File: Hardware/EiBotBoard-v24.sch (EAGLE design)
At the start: 99 parts, among them IC1 A4988ALT1, IC2 A4988ALT1, IC3 PIC18F46J50-I/PT, IC4 V_REG_317DPACK, IC5 V_REG_317DPACK

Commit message: Updated board and schematic as per Peter Lewis' design review nodes (issue #1 in GitHub)
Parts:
- renumbered IC1 to U1, IC2 to U2, IC3 to U3, IC4 to U4, IC5 to U5
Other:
- note added: "Updated as per SparkFun design review #1 (issue 1)"
- note added: "copyright 2011-2015"
- note added: "of Schmalz Haus LLC"
- note added: "v2.4 04/29/2015 - Revision by BPS"
- note removed: "copyright 2011-2013"
- note removed: "of Schmalz Haus"

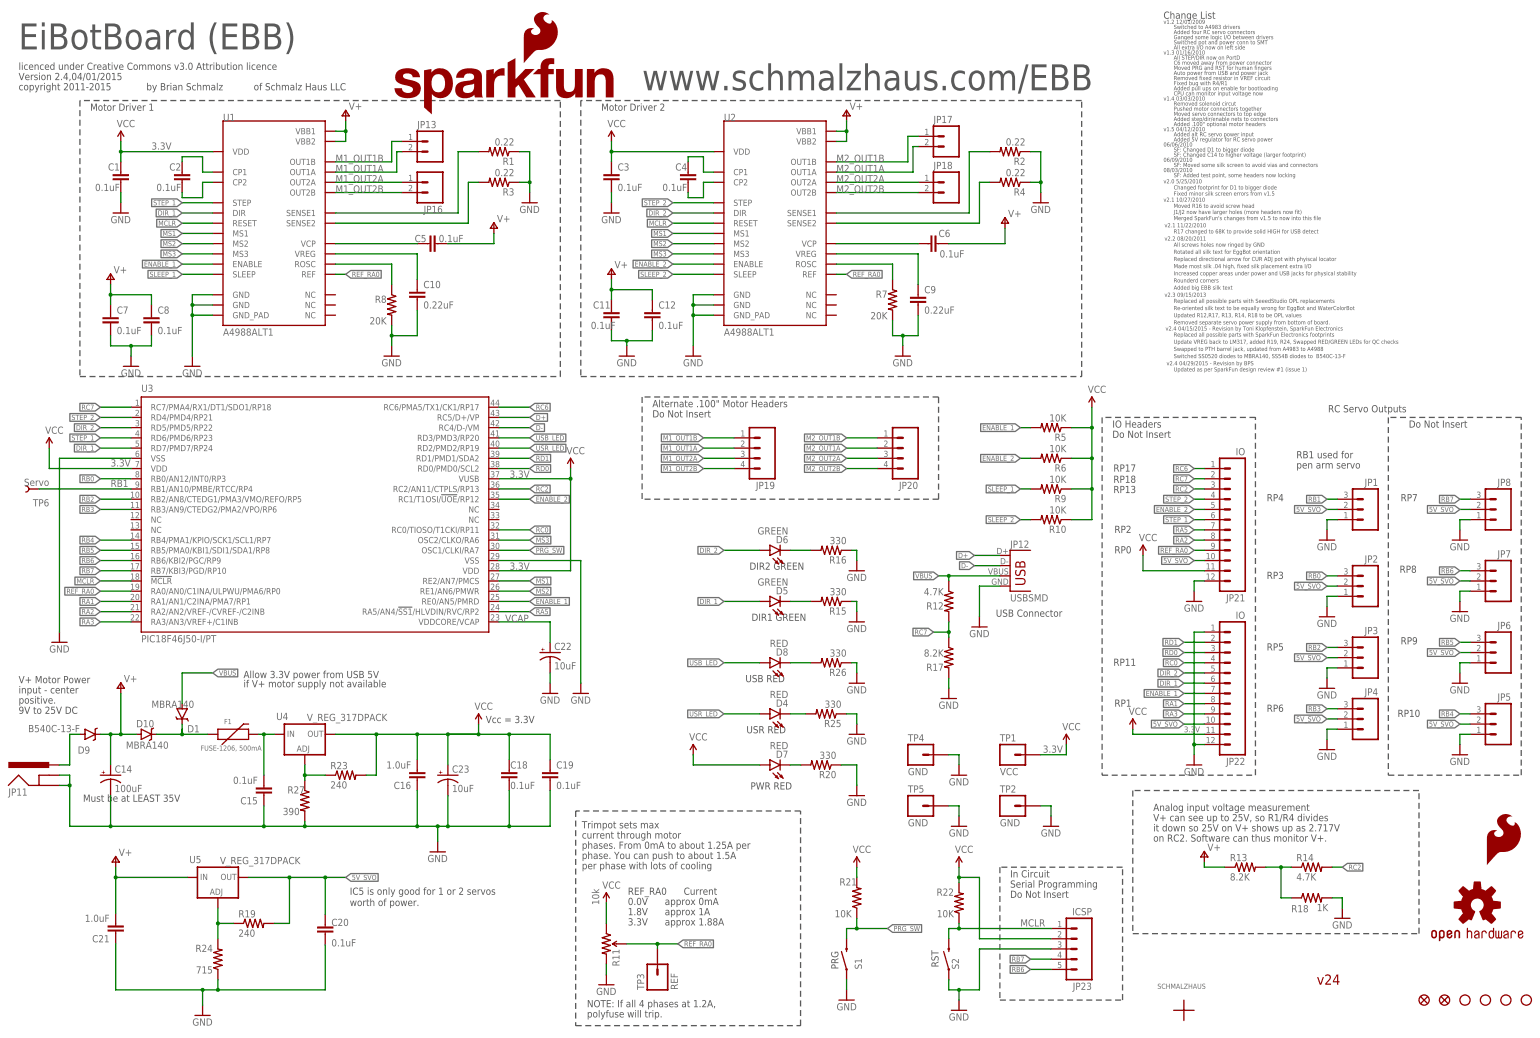
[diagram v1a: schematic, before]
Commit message: Reverted LEDs back to their original colors, removed outline line on tPlace, made outline on dimension layer 0.008" wide, switched driver chip footprints to A4988ALT1_REDUCED_PASTE.
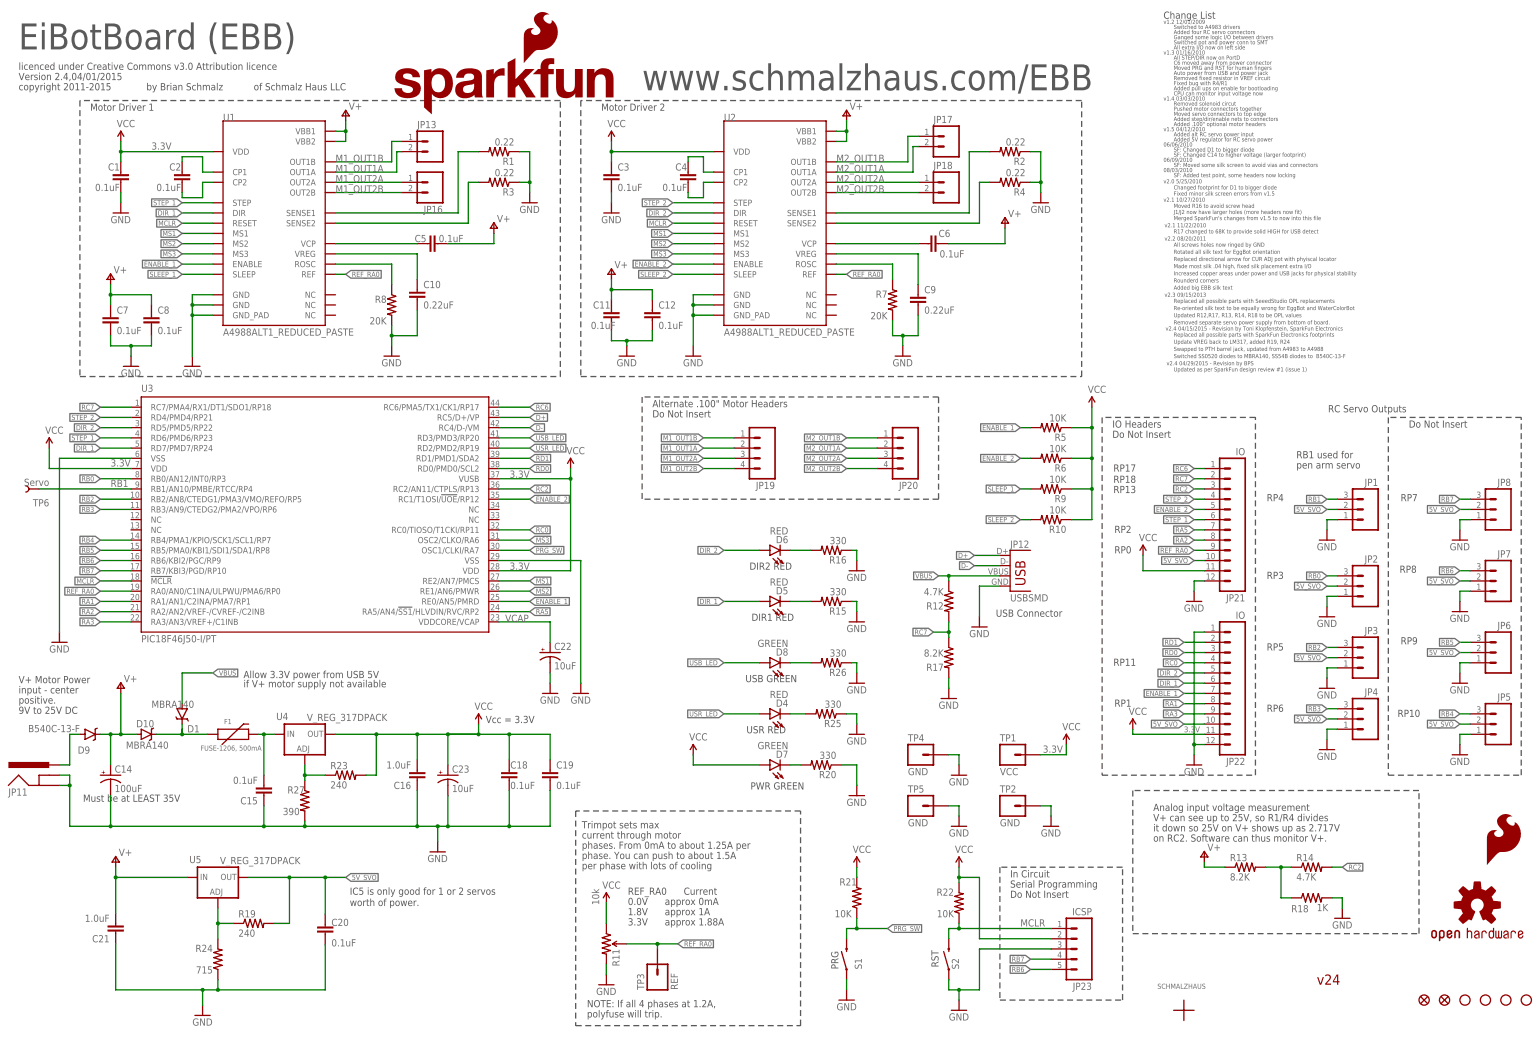
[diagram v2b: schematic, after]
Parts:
- D5, D6: value GREEN -> RED; device SparkFun-LED:LED-GREEN0603 -> SparkFun-LED:LED-RED0603
- D7, D8: value RED -> GREEN; device SparkFun-LED:LED-RED0603 -> SparkFun-LED:LED-GREEN0603
- U1, U2: value A4988ALT1 -> A4988ALT1_REDUCED_PASTE; device SparkFun-PowerIC:A4988ALT1 -> SparkFun-PowerIC:A4988ALT1_REDUCED_PASTE
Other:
- note added: "DIR1 RED"
- note added: "DIR2 RED"
- note added: "PWR GREEN"
- note added: "USB GREEN"
- note added: "Update VREG back to LM317, added R19, R24"
- note removed: "DIR1 GREEN"
- note removed: "DIR2 GREEN"
- note removed: "PWR RED"
- note removed: "USB RED"
- note removed: "Update VREG back to LM317, added R19, R24, Swapped RED/GREEN LEDs for QC checks"

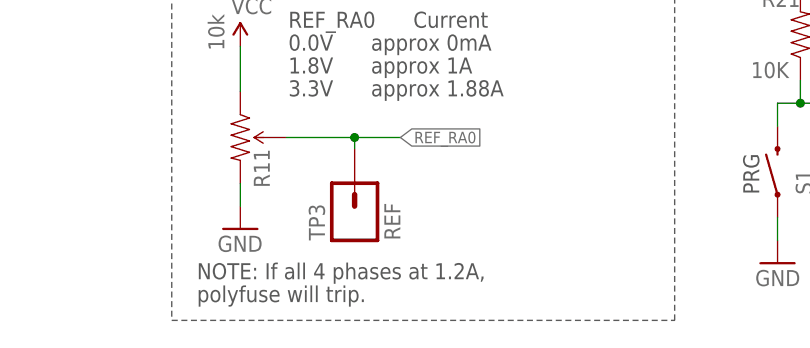
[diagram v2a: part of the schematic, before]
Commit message: Added MAX direction indication on top silk for current adjust pot.
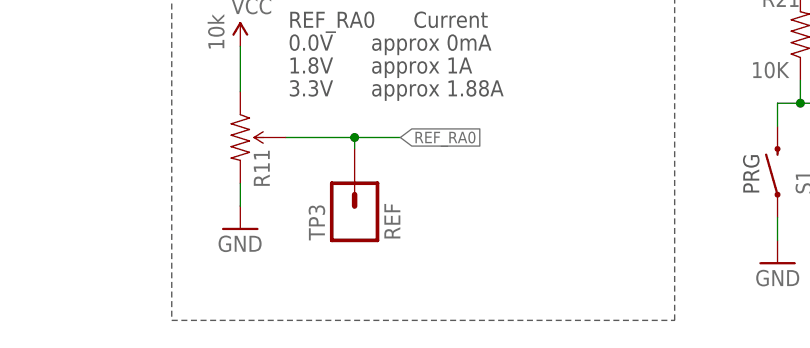
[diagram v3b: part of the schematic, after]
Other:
- note removed: "NOTE: If all 4 phases at 1.2A,"
- note removed: "polyfuse will trip."
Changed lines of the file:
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@@
 <grid distance="0.1" unitdist="inch" unit="inch" style="lines" multiple="1" display="no" altdistance="0.01" altunitdist="inch" altunit="inch"/>
 <layers>
-<layer number="1" name="Top" color="4" fill="1" visible="yes" active="no"/>
-<layer number="2" name="Route2" color="1" fill="3" visible="yes" active="no"/>
-<layer number="3" name="Route3" color="4" fill="3" visible="yes" active="no"/>
-<layer number="4" name="Route4" color="1" fill="4" visible="yes" active="no"/>
-<layer number="5" name="Route5" color="4" fill="4" visible="yes" active="no"/>
-<layer number="6" name="Route6" color="1" fill="8" visible="yes" active="no"/>
-<layer number="7" name="Route7" color="4" fill="8" visible="yes" active="no"/>
-<layer number="8" name="Route8" color="1" fill="2" visible="yes" active="no"/>
-<layer number="9" name="Route9" color="4" fill="2" visible="yes" active="no"/>
-<layer number="10" name="Route10" color="1" fill="7" visible="yes" active="no"/>
-<layer number="11" name="Route11" color="4" fill="7" visible="yes" active="no"/>
-<layer number="12" name="Route12" color="1" fill="5" visible="yes" active="no"/>
-<layer number="13" name="Route13" color="4" fill="5" visible="yes" active="no"/>
-<layer number="14" name="Route14" color="1" fill="6" visible="yes" active="no"/>
-<layer number="15" name="Route15" color="4" fill="6" visible="yes" active="no"/>
-<layer number="16" name="Bottom" color="1" fill="1" visible="yes" active="no"/>
-<layer number="17" name="Pads" color="2" fill="1" visible="yes" active="no"/>
-<layer number="18" name="Vias" color="2" fill="1" visible="yes" active="no"/>
-<layer number="19" name="Unrouted" color="6" fill="1" visible="yes" active="no"/>
-<layer number="20" name="Dimension" color="15" fill="1" visible="yes" active="no"/>
-<layer number="21" name="tPlace" color="16" fill="1" visible="yes" active="no"/>
-<layer number="22" name="bPlace" color="14" fill="1" visible="yes" active="no"/>
-<layer number="23" name="tOrigins" color="15" fill="1" visible="yes" active="no"/>
-<layer number="24" name="bOrigins" color="15" fill="1" visible="yes" active="no"/>
-<layer number="25" name="tNames" color="7" fill="1" visible="yes" active="no"/>
-<layer number="26" name="bNames" color="7" fill="1" visible="yes" active="no"/>
-<layer number="27" name="tValues" color="7" fill="1" visible="yes" active="no"/>
-<layer number="28" name="bValues" color="7" fill="1" visible="yes" active="no"/>
+<layer number="1" name="Top" color="4" fill="1" visible="no" active="no"/>
+<layer number="2" name="Route2" color="1" fill="3" visible="no" active="no"/>
+<layer number="3" name="Route3" color="4" fill="3" visible="no" active="no"/>
+<layer number="4" name="Route4" color="1" fill="4" visible="no" active="no"/>
+<layer number="5" name="Route5" color="4" fill="4" visible="no" active="no"/>
+<layer number="6" name="Route6" color="1" fill="8" visible="no" active="no"/>
+<layer number="7" name="Route7" color="4" fill="8" visible="no" active="no"/>
+<layer number="8" name="Route8" color="1" fill="2" visible="no" active="no"/>
+<layer number="9" name="Route9" color="4" fill="2" visible="no" active="no"/>
+<layer number="10" name="Route10" color="1" fill="7" visible="no" active="no"/>
+<layer number="11" name="Route11" color="4" fill="7" visible="no" active="no"/>
+<layer number="12" name="Route12" color="1" fill="5" visible="no" active="no"/>
+<layer number="13" name="Route13" color="4" fill="5" visible="no" active="no"/>
+<layer number="14" name="Route14" color="1" fill="6" visible="no" active="no"/>
+<layer number="15" name="Route15" color="4" fill="6" visible="no" active="no"/>
+<layer number="16" name="Bottom" color="1" fill="1" visible="no" active="no"/>
+<layer number="17" name="Pads" color="2" fill="1" visible="no" active="no"/>
+<layer number="18" name="Vias" color="2" fill="1" visible="no" active="no"/>
+<layer number="19" name="Unrouted" color="6" fill="1" visible="no" active="no"/>
+<layer number="20" name="Dimension" color="15" fill="1" visible="no" active="no"/>
+<layer number="21" name="tPlace" color="16" fill="1" visible="no" active="no"/>
+<layer number="22" name="bPlace" color="14" fill="1" visible="no" active="no"/>
+<layer number="23" name="tOrigins" color="15" fill="1" visible="no" active="no"/>
+<layer number="24" name="bOrigins" color="15" fill="1" visible="no" active="no"/>
+<layer number="25" name="tNames" color="7" fill="1" visible="no" active="no"/>
+<layer number="26" name="bNames" color="7" fill="1" visible="no" active="no"/>
+<layer number="27" name="tValues" color="7" fill="1" visible="no" active="no"/>
+<layer number="28" name="bValues" color="7" fill="1" visible="no" active="no"/>
 <layer number="29" name="tStop" color="7" fill="3" visible="no" active="no"/>
 <layer number="30" name="bStop" color="7" fill="6" visible="no" active="no"/>
@@
 <layer number="35" name="tGlue" color="7" fill="4" visible="no" active="no"/>
 <layer number="36" name="bGlue" color="7" fill="5" visible="no" active="no"/>
-<layer number="37" name="tTest" color="7" fill="1" visible="yes" active="no"/>
-<layer number="38" name="bTest" color="7" fill="1" visible="yes" active="no"/>
+<layer number="37" name="tTest" color="7" fill="1" visible="no" active="no"/>
+<layer number="38" name="bTest" color="7" fill="1" visible="no" active="no"/>
 <layer number="39" name="tKeepout" color="4" fill="11" visible="no" active="no"/>
 <layer number="40" name="bKeepout" color="1" fill="11" visible="no" active="no"/>
@@
 <layer number="44" name="Drills" color="7" fill="1" visible="no" active="no"/>
 <layer number="45" name="Holes" color="7" fill="1" visible="no" active="no"/>
-<layer number="46" name="Milling" color="3" fill="1" visible="yes" active="no"/>
-<layer number="47" name="Measures" color="7" fill="1" visible="yes" active="no"/>
-<layer number="48" name="Document" color="7" fill="1" visible="yes" active="no"/>
-<layer number="49" name="Reference" color="7" fill="1" visible="yes" active="no"/>
-<layer number="50" name="dxf" color="7" fill="1" visible="yes" active="no"/>
-<layer number="51" name="tDocu" color="6" fill="1" visible="yes" active="no"/>
-<layer number="52" name="bDocu" color="7" fill="1" visible="yes" active="no"/>
-<layer number="53" name="tGND_GNDA" color="7" fill="9" visible="yes" active="no"/>
-<layer number="54" name="bGND_GNDA" color="1" fill="9" visible="yes" active="no"/>
-<layer number="56" name="wert" color="7" fill="1" visible="yes" active="no"/>
-<layer number="57" name="tCAD" color="7" fill="1" visible="yes" active="no"/>
-<layer number="59" name="tCarbon" color="7" fill="1" visible="yes" active="no"/>
-<layer number="60" name="bCarbon" color="7" fill="1" visible="yes" active="no"/>
+<layer number="46" name="Milling" color="3" fill="1" visible="no" active="no"/>
+<layer number="47" name="Measures" color="7" fill="1" visible="no" active="no"/>
+<layer number="48" name="Document" color="7" fill="1" visible="no" active="no"/>
+<layer number="49" name="Reference" color="7" fill="1" visible="no" active="no"/>
+<layer number="50" name="dxf" color="7" fill="1" visible="no" active="no"/>
+<layer number="51" name="tDocu" color="6" fill="1" visible="no" active="no"/>
+<layer number="52" name="bDocu" color="7" fill="1" visible="no" active="no"/>
+<layer number="53" name="tGND_GNDA" color="7" fill="9" visible="no" active="no"/>
+<layer number="54" name="bGND_GNDA" color="1" fill="9" visible="no" active="no"/>
+<layer number="56" name="wert" color="7" fill="1" visible="no" active="no"/>
+<layer number="57" name="tCAD" color="7" fill="1" visible="no" active="no"/>
+<layer number="59" name="tCarbon" color="7" fill="1" visible="no" active="no"/>
+<layer number="60" name="bCarbon" color="7" fill="1" visible="no" active="no"/>
 <layer number="90" name="Modules" color="5" fill="1" visible="yes" active="yes"/>
 <layer number="91" name="Nets" color="2" fill="1" visible="yes" active="yes"/>
@@
 <text x="153.924" y="26.162" size="1.778" layer="97">1.8V      approx 1A</text>
 <text x="18.542" y="54.356" size="1.778" layer="97">Must be at LEAST 35V</text>
-<text x="143.764" y="3.302" size="1.778" layer="97">NOTE: If all 4 phases at 1.2A, </text>
-<text x="143.764" y="0.762" size="1.778" layer="97">polyfuse will trip.</text>
 <text x="287.02" y="220.98" size="1.016" layer="97">v1.5 04/12/2010</text>
 <text x="289.56" y="219.71" size="1.016" layer="97">Added alt RC servo power input</text>
